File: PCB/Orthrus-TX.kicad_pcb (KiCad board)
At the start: 8 copper layers, 49 x 49 mm, 144 parts, among them J1 HRO-TYPE-C-31-M-13x, U2 SRV05-4, U3 SRV05-4, U4 SRV05-4, U5 SRV05-4, U6 SRV05-4, U7 SRV05-4, U8 SRV05-4

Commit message: DRC
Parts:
- moved C5 0.49 mm to (135.1, 53.0)
- moved C42 0.22 mm to (162.6, 52.5)
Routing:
- net /LD1_3.3v: track 291.3 -> 287.9 mm
- net GND: vias 76 -> 77

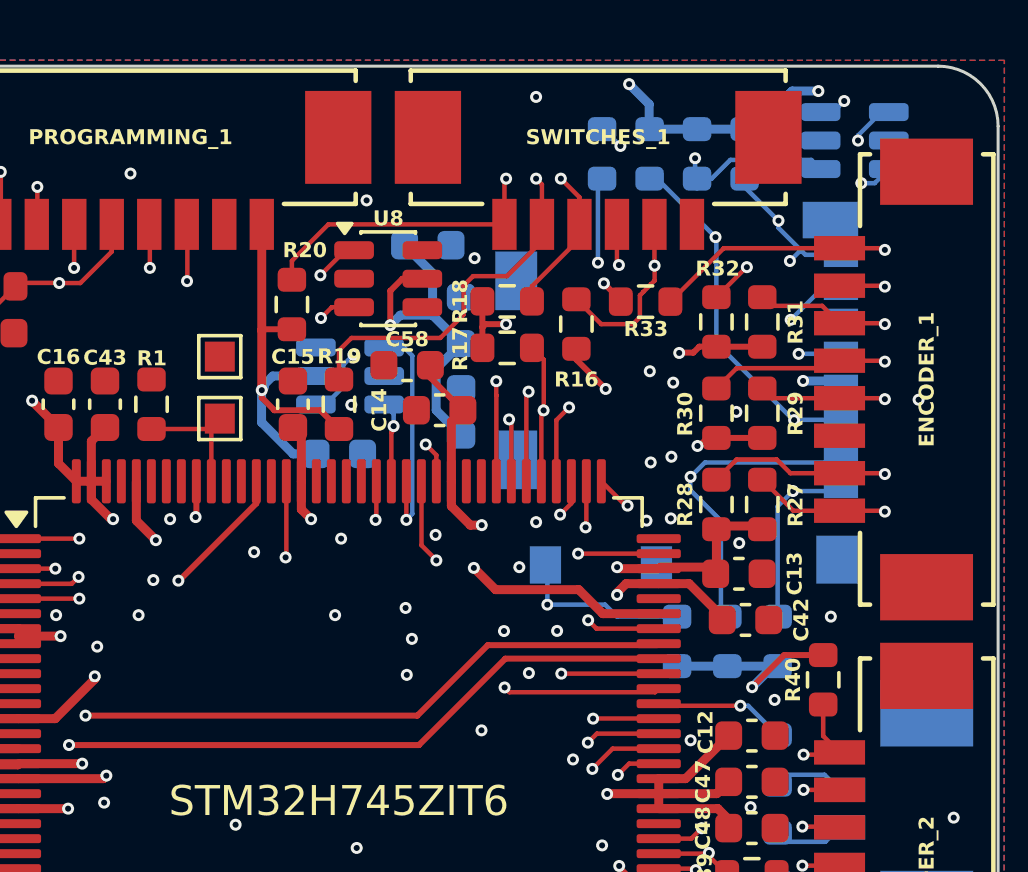
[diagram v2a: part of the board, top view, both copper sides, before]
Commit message: extra LDO for the SDCard
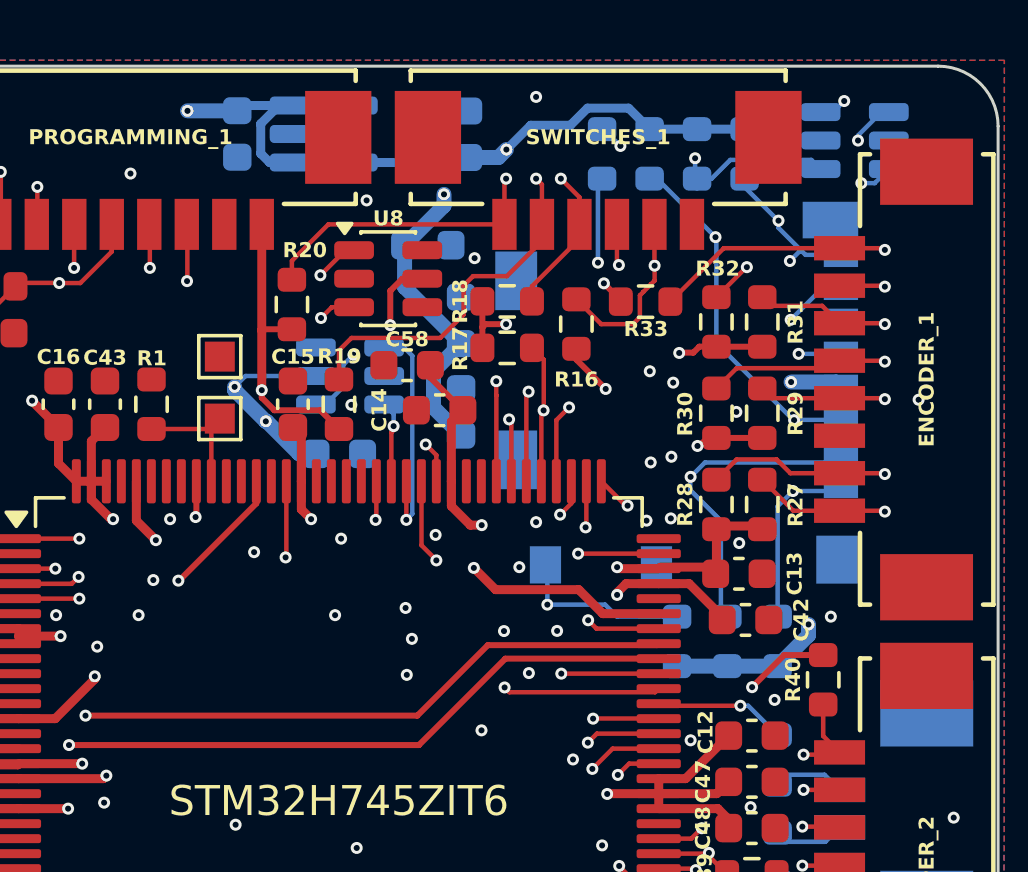
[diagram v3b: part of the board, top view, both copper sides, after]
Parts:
- added C40: 4.7µF, Capacitor_SMD:C_0603_1608Metric, B.Cu at (145.6, 36.3)
- added C59: 2.2µF, Capacitor_SMD:C_0603_1608Metric, B.Cu at (151.8, 36.3)
- added C60: 100nF, Capacitor_SMD:C_0603_1608Metric, B.Cu at (153.3, 36.3)
- added LD4: AP2112K-3.3, Package_TO_SOT_SMD:SOT-23-5, B.Cu at (148.5, 36.3)
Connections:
- C50 pad 1: /LD1_3.3v -> /LD4_3.3v
- C51 pad 1: /LD1_3.3v -> /LD4_3.3v
- C52 pad 2: /LD1_3.3v -> /LD4_3.3v
- C53 pad 2: /LD1_3.3v -> /LD4_3.3v
- R45 pad 2: /LD1_3.3v -> /LD4_3.3v
- R46 pad 2: /LD1_3.3v -> /LD4_3.3v
- R47 pad 2: /LD1_3.3v -> /LD4_3.3v
- R48 pad 1: /LD1_3.3v -> /LD4_3.3v
- R49 pad 1: /LD1_3.3v -> /LD4_3.3v
- R51 pad 1: /LD1_3.3v -> /LD4_3.3v
- SD_CARD_1 pad 4: /LD1_3.3v -> /LD4_3.3v
- U3 pad 5: /LD1_3.3v -> /LD4_3.3v
- U4 pad 5: /LD1_3.3v -> /LD4_3.3v
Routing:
- net /LD4_3.3v: track 0.00 -> 86.7 mm, vias 0 -> 6
- net VCC: track 75.5 -> 104.6 mm, vias 6 -> 7
- net /LD1_3.3v: track 287.9 -> 281.1 mm, vias 37 -> 34
